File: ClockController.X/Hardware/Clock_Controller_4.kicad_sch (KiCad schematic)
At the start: 9 parts, among them J2 HDR-1X2H, Q2 FDD7N25LZTM, Q3 MMBT2222A-TP, Q4 MMBT2907ALT1G

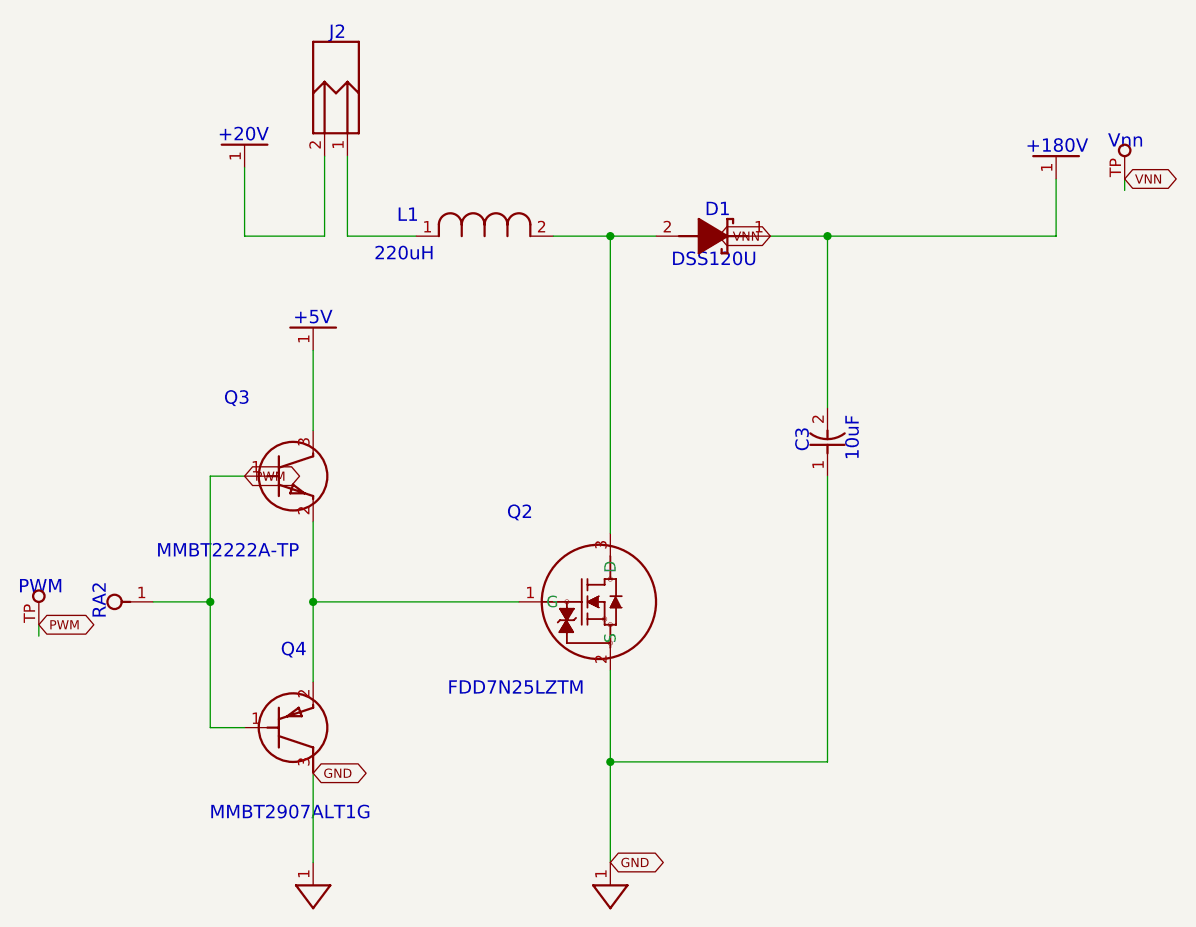
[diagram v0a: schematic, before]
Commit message: Cleaned up a bunch of labels
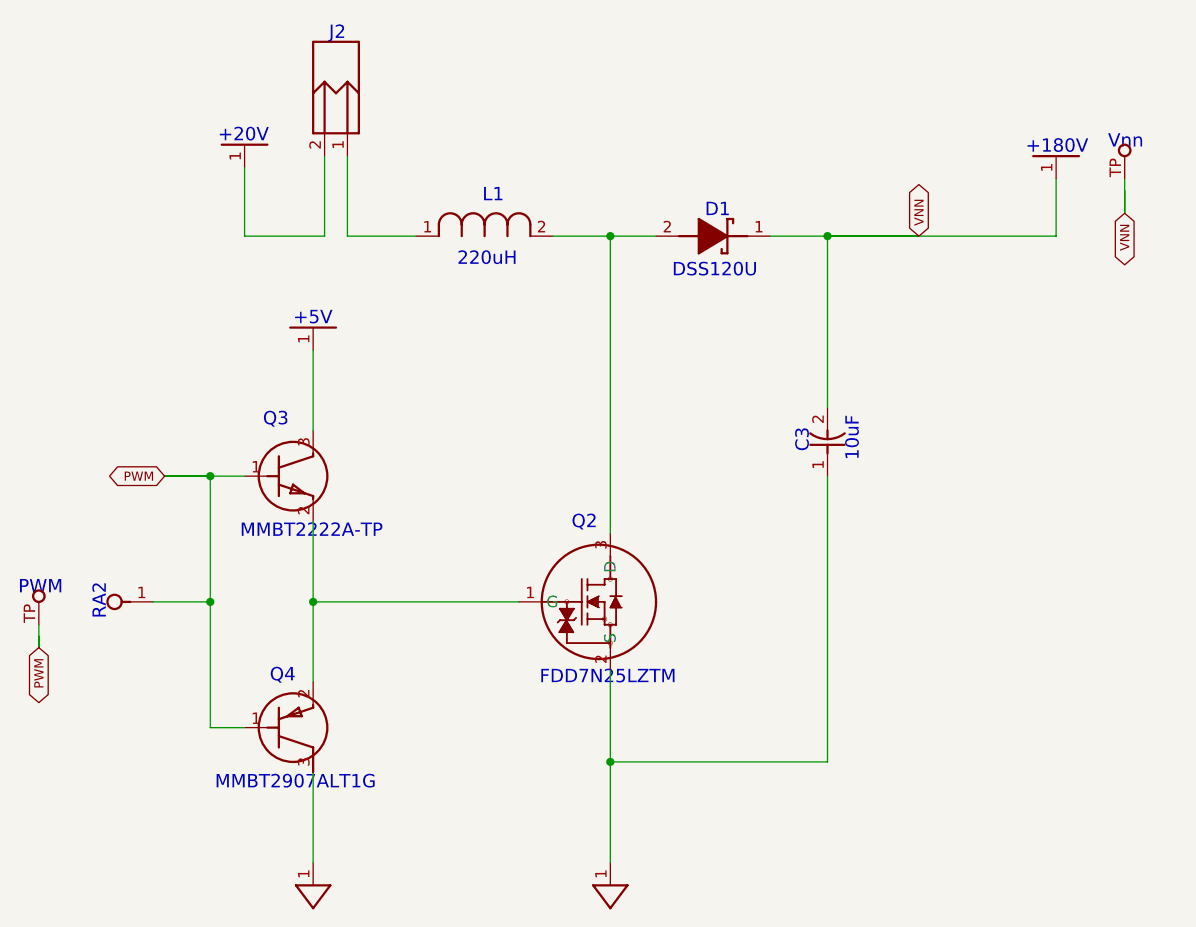
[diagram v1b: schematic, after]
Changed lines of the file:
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@@
+	)
+	(junction
+		(at 104.14 104.14)
+		(diameter 0)
+		(color 0 0 0 0)
 	)
 	(junction
@@
 	(wire
 		(pts
+			(xy 104.14 104.14) (xy 107.95 104.14)
+		)
+		(stroke
+			(width 0)
+			(type default)
+		)
+	)
+	(wire
+		(pts
 			(xy 198.12 77.47) (xy 198.12 71.12)
 		)
@@
 	(wire
 		(pts
+			(xy 205.74 74.93) (xy 205.74 71.12)
+		)
+		(stroke
+			(width 0)
+			(type default)
+		)
+	)
+	(wire
+		(pts
 			(xy 148.59 125.73) (xy 148.59 135.89)
 		)
@@
 	(wire
 		(pts
-			(xy 85.09 120.65) (xy 85.09 121.92)
-		)
-		(stroke
-			(width 0.25)
-			(type solid)
-		)
-	)
-	(wire
-		(pts
-			(xy 205.74 71.12) (xy 205.74 72.39)
+			(xy 85.09 123.19) (xy 85.09 121.92)
+		)
+		(stroke
+			(width 0.25)
+			(type solid)
+		)
+	)
+	(wire
+		(pts
+			(xy 205.74 74.93) (xy 205.74 72.39)
 		)
 		(stroke
@@
 	(wire
 		(pts
-			(xy 107.95 104.14) (xy 104.14 104.14)
+			(xy 99.06 104.14) (xy 104.14 104.14)
 		)
 		(stroke
@@
 	(wire
 		(pts
+			(xy 99.06 104.14) (xy 104.14 104.14)
+		)
+		(stroke
+			(width 0)
+			(type default)
+		)
+	)
+	(wire
+		(pts
+			(xy 148.59 110.49) (xy 148.59 77.47)
+		)
+		(stroke
+			(width 0.25)
+			(type solid)
+		)
+	)
+	(wire
+		(pts
+			(xy 97.79 118.11) (xy 104.14 118.11)
+		)
+		(stroke
+			(width 0.25)
+			(type solid)
+		)
+	)
+	(wire
+		(pts
 			(xy 172.72 77.47) (xy 198.12 77.47)
 		)
@@
 	(wire
 		(pts
-			(xy 148.59 110.49) (xy 148.59 77.47)
-		)
-		(stroke
-			(width 0.25)
-			(type solid)
-		)
-	)
-	(wire
-		(pts
-			(xy 97.79 118.11) (xy 104.14 118.11)
-		)
-		(stroke
-			(width 0.25)
-			(type solid)
-		)
-	)
-	(wire
-		(pts
 			(xy 148.59 77.47) (xy 153.67 77.47)
 		)
@@
 	(wire
 		(pts
-			(xy 166.37 77.47) (xy 172.72 77.47)
-		)
-		(stroke
-			(width 0.25)
-			(type solid)
+			(xy 172.72 77.47) (xy 166.37 77.47)
+		)
+		(stroke
+			(width 0)
+			(type default)
 		)
 	)
@@
 	(wire
 		(pts
+			(xy 85.09 123.19) (xy 85.09 120.65)
+		)
+		(stroke
+			(width 0)
+			(type default)
+		)
+	)
+	(wire
+		(pts
+			(xy 182.88 77.47) (xy 172.72 77.47)
+		)
+		(stroke
+			(width 0)
+			(type default)
+		)
+	)
+	(wire
+		(pts
 			(xy 115.57 137.147) (xy 115.57 147.066)
 		)
@@
 	(text "MMBT2222A-TP"
 		(exclude_from_sim no)
-		(at 98.142 111.76 0)
+		(at 107.442 109.474 0)
 		(effects
 			(font
@@
 	(text "FDD7N25LZTM"
 		(exclude_from_sim no)
-		(at 130.499 127 0)
+		(at 140.716 125.73 0)
 		(effects
 			(font
@@
 	(text "DSS120U"
 		(exclude_from_sim no)
-		(at 155.363 79.375 0)
+		(at 155.448 80.518 0)
 		(effects
 			(font
@@
 	(text "Q2"
 		(exclude_from_sim no)
-		(at 137.101 109.22 0)
+		(at 144.272 110.236 0)
 		(effects
 			(font
@@
 	(text "MMBT2907ALT1G"
 		(exclude_from_sim no)
-		(at 104.058 140.843 0)
+		(at 104.648 137.414 0)
 		(effects
 			(font
@@
 	(text "220uH"
 		(exclude_from_sim no)
-		(at 122.346 78.74 0)
+		(at 131.572 79.248 0)
 		(effects
 			(font
@@
 	(text "Q4"
 		(exclude_from_sim no)
-		(at 111.969 124.46 0)
+		(at 110.744 127.254 0)
 		(effects
 			(font
@@
 	(text "Q3"
 		(exclude_from_sim no)
-		(at 105.655 96.52 0)
+		(at 109.982 98.806 0)
 		(effects
 			(font
@@
 	(text "L1"
 		(exclude_from_sim no)
-		(at 124.875 76.2 0)
+		(at 134.366 73.914 0)
 		(effects
 			(font
@@
 		)
 	)
-	(global_label "GND"
+	(global_label "VNN"
 		(shape bidirectional)
-		(at 148.59 147.066 0)
+		(at 182.88 77.47 90)
 		(fields_autoplaced yes)
 		(effects
@@
 		)
 		(property "Intersheetrefs" "${INTERSHEET_REFS}"
-			(at 154.9633 147.066 0)
+			(at 182.88 71.1934 90)
 			(effects
 				(font
@@
 		)
 	)
-	(global_label "VNN"
+	(global_label "PWM"
 		(shape bidirectional)
-		(at 166.37 77.47 180)
+		(at 85.09 123.19 270)
 		(fields_autoplaced yes)
 		(effects
@@
 		)
 		(property "Intersheetrefs" "${INTERSHEET_REFS}"
-			(at 160.0934 77.47 0)
+			(at 85.09 129.8051 90)
 			(effects
 				(font
@@
 		)
 	)
-	(global_label "PWM"
+	(global_label "VNN"
 		(shape bidirectional)
-		(at 85.09 120.65 0)
+		(at 205.74 74.93 270)
 		(fields_autoplaced yes)
 		(effects
@@
 				(size 1.016 1.016)
 			)
-			(justify left)
+			(justify right)
 		)
 		(property "Intersheetrefs" "${INTERSHEET_REFS}"
-			(at 91.7051 120.65 0)
+			(at 205.74 81.2066 90)
 			(effects
 				(font
 					(size 1.27 1.27)
 				)
-				(justify left)
+				(justify right)
 				(hide yes)
 			)
 		)
 	)
-	(global_label "VNN"
+	(global_label "PWM"
 		(shape bidirectional)
-		(at 205.74 71.12 0)
+		(at 99.06 104.14 180)
 		(fields_autoplaced yes)
 		(effects
@@
 				(size 1.016 1.016)
 			)
-			(justify left)
+			(justify right)
 		)
 		(property "Intersheetrefs" "${INTERSHEET_REFS}"
-			(at 212.0166 71.12 0)
+			(at 92.4449 104.14 0)
 			(effects
 				(font
 					(size 1.27 1.27)
 				)
-				(justify left)
+				(justify right)
 				(hide yes)
 			)
-		)
-	)
-	(global_label "GND"
-		(shape bidirectional)
-		(at 115.57 137.147 0)
-		(fields_autoplaced yes)
-		(effects
-			(font
-				(size 1.016 1.016)
-			)
-			(justify left)
-		)
-		(property "Intersheetrefs" "${INTERSHEET_REFS}"
-			(at 121.9433 137.147 0)
-			(effects
-				(font
-					(size 1.27 1.27)
-				)
-				(justify left)
-				(hide yes)
-			)
-		)
-	)
-	(global_label "PWM"
-		(shape bidirectional)
-		(at 107.95 104.14 0)
-		(fields_autoplaced yes)
-		(effects
-			(font
-				(size 1.016 1.016)
-			)
-			(justify left)
-		)
-		(property "Intersheetrefs" "${INTERSHEET_REFS}"
-			(at 114.5651 104.14 0)
-			(effects
-				(font
-					(size 1.27 1.27)
-				)
-				(justify left)
-				(hide yes)
-			)
